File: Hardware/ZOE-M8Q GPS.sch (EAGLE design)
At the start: 23 parts, among them J4 U.FL, U1 UBLOX_ZOE_M8-0-10, Y1 32.768kHz

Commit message: Adds Buzzard Labels, finishes tracework (see description)
* Moves diode and reistor
* Fixes TSTOP on LGA
* Moves uFL connector
* Moves Jumpers
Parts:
- removed H1: STAND-OFFTIGHT, SparkFun-Hardware:STAND-OFFTIGHT
- added JP1: JUMPER-SMT_2_NO_SILK, SparkFun-Jumpers:JUMPER-SMT_2_NO_SILK
- added LOGO1: SFE_LOGO_NAME.1_INCH, SparkFun-Aesthetics:SFE_LOGO_NAME.1_INCH
- added LOGO2: OSHW-LOGOS, SparkFun-Aesthetics:OSHW-LOGOS
- added LOGO3: SFE_LOGO_FLAME.1_INCH, SparkFun-Aesthetics:SFE_LOGO_FLAME.1_INCH
- J3: device SparkFun-Connectors:CONN_05NO_SILK -> SparkFun-Connectors:CONN_06NO_SILK_NO_POP
- J5: device SparkFun-Connectors:CONN_05NO_SILK -> SparkFun-Connectors:CONN_041X04_NO_SILK
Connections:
- removed net LNA_EN: U1.LNA_EN
- removed net N$16: U1.P1015
- removed net N$4: JP2.1, R4.2
- removed net N$9: U1.P1014
- removed net RXD/MOSI: U1.RXD/MOSI
- removed net TXD/MISO: U1.TXD/MISO
- new net N$1: JP2.1, R3.2
- new net RXI/MOSI: J3.4, U1.RXD/MOSI
- new net TXO/MISO: J3.5, U1.TXD/MISO
- net 3.3V: now also J3.1
- net D_SEL: now also JP1.1
- net GND: now also J3.6, JP1.2
- net INT: now also J5.1
- net N$3: now also R4.2; no longer R3.2
- net RESET: now also J5.2
- net SAFEBOOT: now also J5.4
- net SCL/CLK: now also J3.3
- net SDA/CS: now also J3.2
- net TIMEPULSE: now also J5.3
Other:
- note added: "Battery"
- note added: "Close Jumper for SPI"
- note added: "Connectors"
- note added: "I2C Pull ups"
- note added: "Jumpers"
- note added: "uBlox ZOE-M8Q-0-10"
- note added: "v01"
- note removed: "v10"
- moved on the sheet: BT1, C1, D1, J1, J2, J4, JP2, L1, R1, R3, R4, U1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

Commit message: Updates silk, adds new inductor, adds LED
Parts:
- removed L1: 2.2µH/±20%/1.5A, SparkFun-Coils:INDUCTOR-VLF4012AT-2.2UH
- added D2: RED, SparkFun-LED:LED-RED0603
- added JP4: JUMPER-SMT_2_NC_TRACE_SILK, SparkFun-Jumpers:JUMPER-SMT_2_NC_TRACE_SILK
- added R2: 1k, SparkFun-Resistors:1KOHM-0603-1/10W-1%
- added U$20: 2.2UH_SHIELDED_INDUCTOR, temp:2.2UH_SHIELDED_INDUCTOR
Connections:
- new net N$4: D2.A, R2.1
- new net N$8: D2.C, JP4.2
- net 3.3V: now also J3.3, R2.2; no longer J3.1
- net GND: now also JP4.1
- net N$6: now also U$20.1; no longer L1.1
- net N$7: now also U$20.2; no longer L1.2
- net SCL/CLK: now also J3.1; no longer J3.3
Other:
- note added: "Cut trace to disconnect LED"
- note added: "FTDI"
- note added: "I2C standard"
- note added: "UART Connector"
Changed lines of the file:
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@@
 <class number="0" name="default" width="0" drill="0">
+</class>
+<class number="1" name="smallAnnular" width="0" drill="0">
 </class>
 </classes>
@@
 <part name="J4" library="SparkFun-Connectors" deviceset="U.FL2PIN" device="" value="U.FL"/>
 <part name="C1" library="SparkFun-Capacitors" deviceset="4.7UF" device="-0603-6.3V-(10%)" value="4.7uF"/>
-<part name="L1" library="SparkFun-Coils" deviceset="INDUCTOR" device="-VLF4012AT-2.2UH" value="2.2µH/±20%/1.5A"/>
 <part name="Y1" library="SparkFun-Clocks" deviceset="CRYSTAL-32.768KHZ" device="SMD-3.2X1.5" value="32.768kHz"/>
 <part name="SUPPLY2" library="SparkFun-PowerSymbols" deviceset="3.3V" device=""/>
@@
 <part name="LOGO2" library="SparkFun-Aesthetics" deviceset="OSHW-LOGO" device="S" value="OSHW-LOGOS"/>
 <part name="LOGO3" library="SparkFun-Aesthetics" deviceset="SFE_LOGO_FLAME" device=".1_INCH"/>
+<part name="D2" library="SparkFun-LED" deviceset="LED-RED" device="0603" value="RED"/>
+<part name="R2" library="SparkFun-Resistors" deviceset="1KOHM" device="-0603-1/10W-1%" value="1k"/>
+<part name="SUPPLY7" library="SparkFun-PowerSymbols" deviceset="3.3V" device=""/>
+<part name="GND5" library="SparkFun-PowerSymbols" deviceset="GND" device=""/>
+<part name="U$20" library="temp" deviceset="2.2UH_SHIELDED_INDUCTOR" device=""/>
+<part name="JP4" library="SparkFun-Jumpers" deviceset="JUMPER-SMT_2_NC_TRACE" device="_SILK" value="JUMPER-SMT_2_NC_TRACE_SILK"/>
 </parts>
 <sheets>
@@
 <text x="327.66" y="160.02" size="2.54" layer="97" font="vector">Close Jumper for SPI</text>
 <text x="396.24" y="157.48" size="2.54" layer="97" font="vector">I2C Pull ups</text>
+<text x="233.68" y="177.8" size="2.54" layer="97" font="vector">FTDI </text>
+<text x="233.68" y="172.72" size="2.54" layer="97" font="vector">I2C standard</text>
+<text x="233.68" y="182.88" size="2.54" layer="97" font="vector">UART Connector</text>
+<text x="335.28" y="99.06" size="2.54" layer="97" font="vector">Cut trace to disconnect LED</text>
 </plain>
 <instances>
@@
 <attribute name="VALUE" x="29.464" y="195.961" size="1.778" layer="96" font="vector"/>
 </instance>
-<instance part="L1" gate="G$1" x="38.1" y="210.82" smashed="yes" rot="R90">
-<attribute name="NAME" x="39.37" y="213.36" size="1.778" layer="95" font="vector" rot="R180"/>
-<attribute name="VALUE" x="49.53" y="208.28" size="1.778" layer="96" font="vector" rot="R180" align="top-left"/>
-</instance>
 <instance part="Y1" gate="G$1" x="106.68" y="203.2" smashed="yes" rot="MR90">
 <attribute name="NAME" x="104.648" y="204.724" size="1.778" layer="95" font="vector" rot="MR0" align="bottom-center"/>
@@
 <instance part="LOGO2" gate="G$1" x="398.78" y="45.72" smashed="yes"/>
 <instance part="LOGO3" gate="G$1" x="353.06" y="48.26" smashed="yes"/>
+<instance part="D2" gate="G$1" x="332.74" y="114.3" smashed="yes">
+<attribute name="NAME" x="329.311" y="109.728" size="1.778" layer="95" font="vector" rot="R90"/>
+<attribute name="VALUE" x="334.645" y="109.728" size="1.778" layer="96" font="vector" rot="R90" align="top-left"/>
+</instance>
+<instance part="R2" gate="G$1" x="332.74" y="124.46" smashed="yes" rot="R90">
+<attribute name="NAME" x="331.216" y="124.46" size="1.778" layer="95" font="vector" rot="R90" align="bottom-center"/>
+<attribute name="VALUE" x="334.264" y="124.46" size="1.778" layer="96" font="vector" rot="R90" align="top-center"/>
+</instance>
+<instance part="SUPPLY7" gate="G$1" x="332.74" y="132.08" smashed="yes">
+<attribute name="VALUE" x="332.74" y="134.874" size="1.778" layer="96" align="bottom-center"/>
+</instance>
+<instance part="GND5" gate="1" x="332.74" y="91.44" smashed="yes">
+<attribute name="VALUE" x="332.74" y="91.186" size="1.778" layer="96" align="top-center"/>
+</instance>
+<instance part="U$20" gate="G$1" x="38.1" y="210.82" smashed="yes" rot="R90">
+<attribute name="NAME" x="34.29" y="208.28" size="1.778" layer="95" font="vector" rot="R180"/>
+<attribute name="VALUE" x="40.64" y="212.09" size="1.778" layer="96" font="vector" rot="R90" align="top-left"/>
+</instance>
+<instance part="JP4" gate="G$1" x="332.74" y="101.6" smashed="yes" rot="R90">
+<attribute name="NAME" x="340.36" y="104.14" size="1.778" layer="95" font="vector" rot="R180"/>
+</instance>
 </instances>
 <busses>
@@
 </segment>
 <segment>
+<pinref part="GND4" gate="1" pin="GND"/>
 <wire x1="248.92" y1="154.94" x2="248.92" y2="139.7" width="0.1524" layer="91"/>
-<pinref part="GND4" gate="1" pin="GND"/>
 <pinref part="J3" gate="G$1" pin="6"/>
 <wire x1="243.84" y1="154.94" x2="248.92" y2="154.94" width="0.1524" layer="91"/>
+</segment>
+<segment>
+<pinref part="GND5" gate="1" pin="GND"/>
+<wire x1="332.74" y1="93.98" x2="332.74" y2="96.52" width="0.1524" layer="91"/>
+<pinref part="JP4" gate="G$1" pin="1"/>
 </segment>
 </net>
@@
 </segment>
 <segment>
-<pinref part="J3" gate="G$1" pin="1"/>
 <pinref part="SUPPLY4" gate="G$1" pin="3.3V"/>
-<wire x1="243.84" y1="142.24" x2="251.46" y2="142.24" width="0.1524" layer="91"/>
-<wire x1="251.46" y1="142.24" x2="251.46" y2="154.94" width="0.1524" layer="91"/>
+<wire x1="251.46" y1="147.32" x2="251.46" y2="154.94" width="0.1524" layer="91"/>
+<pinref part="J3" gate="G$1" pin="3"/>
+<wire x1="243.84" y1="147.32" x2="251.46" y2="147.32" width="0.1524" layer="91"/>
+</segment>
+<segment>
+<pinref part="SUPPLY7" gate="G$1" pin="3.3V"/>
+<pinref part="R2" gate="G$1" pin="2"/>
+<wire x1="332.74" y1="132.08" x2="332.74" y2="129.54" width="0.1524" layer="91"/>
 </segment>
 </net>
@@
 </segment>
 <segment>
-<pinref part="J3" gate="G$1" pin="3"/>
-<wire x1="243.84" y1="147.32" x2="254" y2="147.32" width="0.1524" layer="91"/>
-<label x="254" y="147.32" size="1.27" layer="95" font="vector" xref="yes"/>
+<pinref part="J3" gate="G$1" pin="1"/>
+<wire x1="243.84" y1="142.24" x2="254" y2="142.24" width="0.1524" layer="91"/>
+<label x="254" y="142.24" size="1.27" layer="95" font="vector" xref="yes"/>
 </segment>
 </net>
@@
 <pinref part="U1" gate="G$1" pin="V_DCDC_OUT"/>
 <wire x1="45.72" y1="210.82" x2="43.18" y2="210.82" width="0.1524" layer="91"/>
-<pinref part="L1" gate="G$1" pin="2"/>
+<pinref part="U$20" gate="G$1" pin="2"/>
 </segment>
 </net>
 <net name="N$6" class="0">
 <segment>
-<pinref part="L1" gate="G$1" pin="1"/>
 <wire x1="33.02" y1="210.82" x2="27.94" y2="210.82" width="0.1524" layer="91"/>
 <wire x1="27.94" y1="210.82" x2="27.94" y2="213.36" width="0.1524" layer="91"/>
@@
 <wire x1="27.94" y1="210.82" x2="27.94" y2="203.2" width="0.1524" layer="91"/>
 <junction x="27.94" y="210.82"/>
+<pinref part="U$20" gate="G$1" pin="1"/>
 </segment>
 </net>
@@
 </segment>
 </net>
+<net name="N$4" class="0">
+<segment>
+<pinref part="D2" gate="G$1" pin="A"/>
+<pinref part="R2" gate="G$1" pin="1"/>
+<wire x1="332.74" y1="116.84" x2="332.74" y2="119.38" width="0.1524" layer="91"/>
+</segment>
+</net>
+<net name="N$8" class="0">
+<segment>
+<pinref part="D2" gate="G$1" pin="C"/>
+<wire x1="332.74" y1="106.68" x2="332.74" y2="109.22" width="0.1524" layer="91"/>
+<pinref part="JP4" gate="G$1" pin="2"/>
+</segment>
+</net>

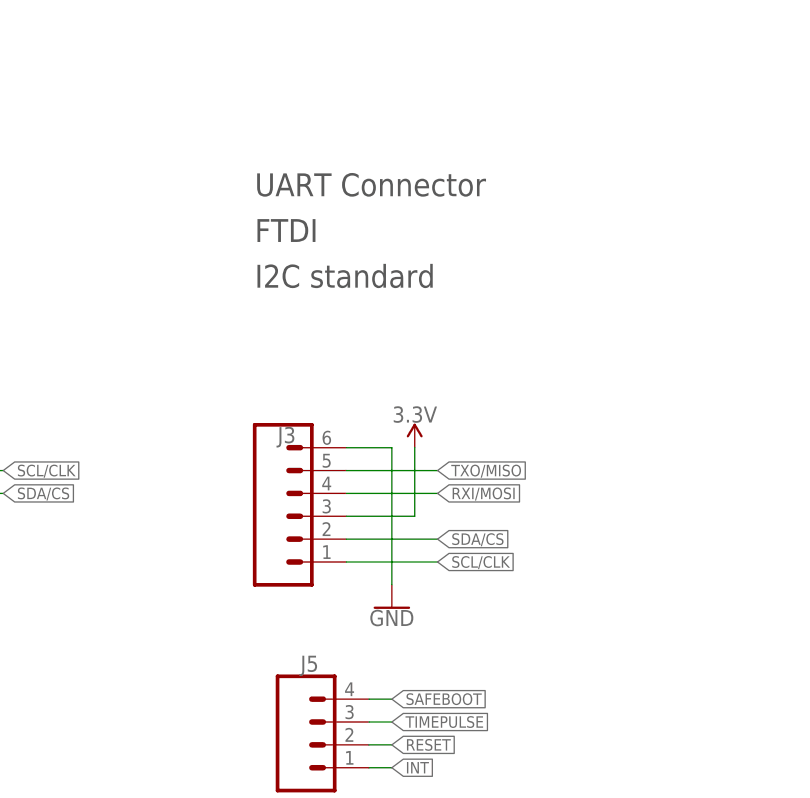
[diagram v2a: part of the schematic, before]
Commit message: Adds pinout for FTDI connection, updates NDUC and ZOE footprints with tkeepout and tdocu, fixes silk labels
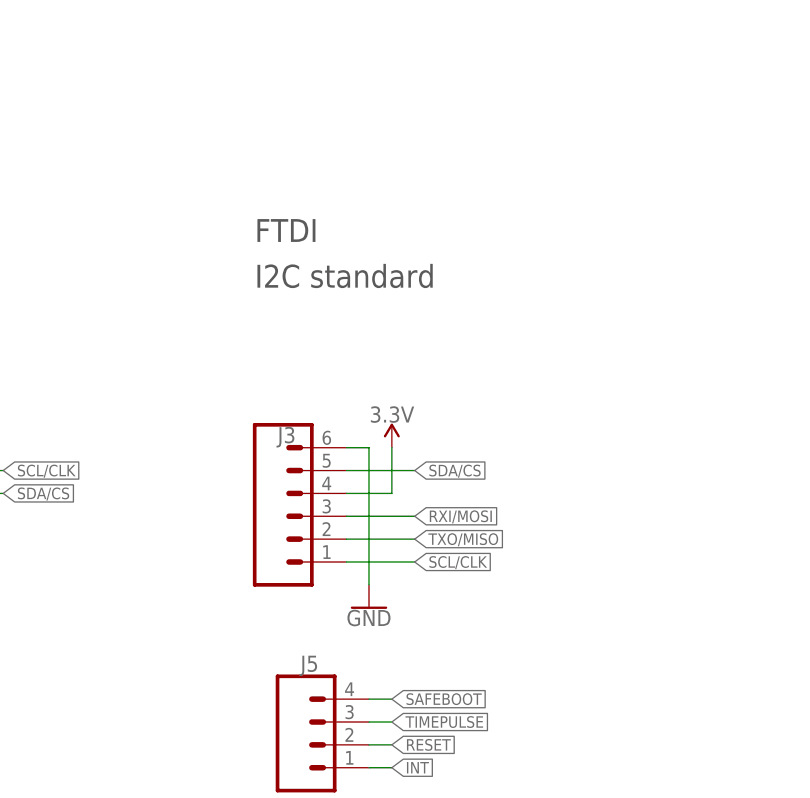
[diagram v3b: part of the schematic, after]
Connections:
- net 3.3V: now also J3.4; no longer J3.3
- net RXI/MOSI: now also J3.3; no longer J3.4
- net SDA/CS: now also J3.5; no longer J3.2
- net TXO/MISO: now also J3.2; no longer J3.5
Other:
- note removed: "UART Connector"
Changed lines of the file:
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@@
 <text x="233.68" y="177.8" size="2.54" layer="97" font="vector">FTDI </text>
 <text x="233.68" y="172.72" size="2.54" layer="97" font="vector">I2C standard</text>
-<text x="233.68" y="182.88" size="2.54" layer="97" font="vector">UART Connector</text>
 <text x="335.28" y="99.06" size="2.54" layer="97" font="vector">Cut trace to disconnect LED</text>
 </plain>
@@
 <attribute name="VALUE" x="350.52" y="147.066" size="1.778" layer="96" align="top-center"/>
 </instance>
-<instance part="SUPPLY4" gate="G$1" x="251.46" y="154.94" smashed="yes">
-<attribute name="VALUE" x="251.46" y="157.734" size="1.778" layer="96" align="bottom-center"/>
-</instance>
-<instance part="GND4" gate="1" x="248.92" y="137.16" smashed="yes">
-<attribute name="VALUE" x="248.92" y="136.906" size="1.778" layer="96" align="top-center"/>
+<instance part="SUPPLY4" gate="G$1" x="248.92" y="154.94" smashed="yes">
+<attribute name="VALUE" x="248.92" y="157.734" size="1.778" layer="96" align="bottom-center"/>
+</instance>
+<instance part="GND4" gate="1" x="246.38" y="137.16" smashed="yes">
+<attribute name="VALUE" x="246.38" y="136.906" size="1.778" layer="96" align="top-center"/>
 </instance>
 <instance part="LOGO1" gate="G$1" x="327.66" y="33.02" smashed="yes"/>
@@
 <segment>
 <pinref part="GND4" gate="1" pin="GND"/>
-<wire x1="248.92" y1="154.94" x2="248.92" y2="139.7" width="0.1524" layer="91"/>
+<wire x1="246.38" y1="154.94" x2="246.38" y2="139.7" width="0.1524" layer="91"/>
 <pinref part="J3" gate="G$1" pin="6"/>
-<wire x1="243.84" y1="154.94" x2="248.92" y2="154.94" width="0.1524" layer="91"/>
+<wire x1="243.84" y1="154.94" x2="246.38" y2="154.94" width="0.1524" layer="91"/>
 </segment>
 <segment>
@@
 <segment>
 <pinref part="SUPPLY4" gate="G$1" pin="3.3V"/>
-<wire x1="251.46" y1="147.32" x2="251.46" y2="154.94" width="0.1524" layer="91"/>
-<pinref part="J3" gate="G$1" pin="3"/>
-<wire x1="243.84" y1="147.32" x2="251.46" y2="147.32" width="0.1524" layer="91"/>
+<pinref part="J3" gate="G$1" pin="4"/>
+<wire x1="248.92" y1="149.86" x2="248.92" y2="154.94" width="0.1524" layer="91"/>
+<wire x1="243.84" y1="149.86" x2="248.92" y2="149.86" width="0.1524" layer="91"/>
 </segment>
 <segment>
@@
 </segment>
 <segment>
-<pinref part="J3" gate="G$1" pin="2"/>
-<wire x1="243.84" y1="144.78" x2="254" y2="144.78" width="0.1524" layer="91"/>
-<label x="254" y="144.78" size="1.27" layer="95" font="vector" xref="yes"/>
+<pinref part="J3" gate="G$1" pin="5"/>
+<wire x1="243.84" y1="152.4" x2="251.46" y2="152.4" width="0.1524" layer="91"/>
+<label x="251.46" y="152.4" size="1.27" layer="95" xref="yes"/>
 </segment>
 </net>
@@
 <segment>
 <pinref part="J3" gate="G$1" pin="1"/>
-<wire x1="243.84" y1="142.24" x2="254" y2="142.24" width="0.1524" layer="91"/>
-<label x="254" y="142.24" size="1.27" layer="95" font="vector" xref="yes"/>
+<wire x1="243.84" y1="142.24" x2="251.46" y2="142.24" width="0.1524" layer="91"/>
+<label x="251.46" y="142.24" size="1.27" layer="95" font="vector" xref="yes"/>
 </segment>
 </net>
@@
 </segment>
 <segment>
-<pinref part="J3" gate="G$1" pin="5"/>
-<wire x1="243.84" y1="152.4" x2="254" y2="152.4" width="0.1524" layer="91"/>
-<label x="254" y="152.4" size="1.27" layer="95" font="vector" xref="yes"/>
+<pinref part="J3" gate="G$1" pin="2"/>
+<wire x1="243.84" y1="144.78" x2="251.46" y2="144.78" width="0.1524" layer="91"/>
+<label x="251.46" y="144.78" size="1.27" layer="95" xref="yes"/>
 </segment>
 </net>
@@
 </segment>
 <segment>
-<pinref part="J3" gate="G$1" pin="4"/>
-<wire x1="243.84" y1="149.86" x2="254" y2="149.86" width="0.1524" layer="91"/>
-<label x="254" y="149.86" size="1.27" layer="95" font="vector" xref="yes"/>
-</segment>
-</net>
+<pinref part="J3" gate="G$1" pin="3"/>
+<wire x1="243.84" y1="147.32" x2="251.46" y2="147.32" width="0.1524" layer="91"/>
+<label x="251.46" y="147.32" size="1.27" layer="95" xref="yes"/>
+</segment>
+</net>

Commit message: Removes one qwiic connector to make space for super capacitor, adds active antenna components (see description)
* Adds 10 ohm resistor, ferrite bead, and 47pF capacitor.
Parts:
- removed BT1: 6.8MM_COIN_CELL, SparkFun-Batteries:BATTERY-6.8MM_SMD
- removed J2: (no value), SparkFun-Connectors:QWIIC_CONNECTORJS-1MM
- added C2: .22F-SUPERCAP, SparkFun-Capacitors:.22F-SUPERCAP
- added C3: 47pF, SparkFun-Capacitors:47PF-0603-50V-5%
- added FB1: FERRITE_BEAD-120_OHM-0402, SparkFun-Coils:FERRITE_BEAD-120_OHM-0402
- added R5: 10, SparkFun-Resistors:10OHM-0603-1/10W-1%
- LOGO1: value SFE_LOGO_NAME.1_INCH -> SFE_LOGO_NAME_FLAME.1_INCH; device SparkFun-Aesthetics:SFE_LOGO_NAME.1_INCH -> SparkFun-Aesthetics:SFE_LOGO_NAME_FLAME.1_INCH
- renumbered U$20 to L1
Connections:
- removed net N$5: J4.SIGNAL, U1.RF_IN
- new net ANT: FB1.1, J4.SIGNAL, U1.RF_IN
- new net N$9: C3.1, FB1.2, R5.1
- net 3.3V: now also R5.2; no longer J2.2
- net GND: now also C2.-, C3.2; no longer BT1.-, J2.1
- net SCL/CLK: no longer J2.4
- net SDA/CS: no longer J2.3
- net V_BATT: now also C2.+; no longer BT1.+
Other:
- note added: "Antenna"
- note added: "Super Capacitor"
- note removed: "Battery"
- moved on the sheet: D2, J1, J3, J4, J5, JP1, JP2, JP4, R2, R3, R4

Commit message: Adds more ground stitching vias
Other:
- note removed: "FTDI"
- note removed: "I2C standard"
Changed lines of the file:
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@@
 <text x="322.58" y="238.76" size="2.54" layer="97" font="vector">Close Jumper for SPI</text>
 <text x="391.16" y="236.22" size="2.54" layer="97" font="vector">I2C Pull ups</text>
-<text x="233.68" y="106.68" size="2.54" layer="97" font="vector">FTDI </text>
-<text x="233.68" y="101.6" size="2.54" layer="97" font="vector">I2C standard</text>
 <text x="330.2" y="177.8" size="2.54" layer="97" font="vector">Cut trace to disconnect LED</text>
 <wire x1="132.08" y1="129.54" x2="302.26" y2="129.54" width="0.2032" layer="97" style="shortdash"/>

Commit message: Adds traces for unconnected ground pins, and changes 1k resistor to 100
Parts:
- R1: value 1k -> 100; device SparkFun-Resistors:1KOHM-0603-1/10W-1% -> SparkFun-Resistors:100OHM-0603-1/10W-1%
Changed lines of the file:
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@@
 <part name="J5" library="SparkFun-Connectors" deviceset="CONN_04" device="1X04_NO_SILK"/>
 <part name="D1" library="SparkFun-DiscreteSemi" deviceset="DIODE-SCHOTTKY" device="-PMEG4005EJ" value="0.5A/40V/420mV"/>
-<part name="R1" library="SparkFun-Resistors" deviceset="1KOHM" device="-0603-1/10W-1%" value="1k"/>
+<part name="R1" library="SparkFun-Resistors" deviceset="100OHM" device="-0603-1/10W-1%" value="100"/>
 <part name="SUPPLY1" library="SparkFun-PowerSymbols" deviceset="V_BATT" device=""/>
 <part name="SUPPLY3" library="SparkFun-PowerSymbols" deviceset="3.3V" device=""/>
